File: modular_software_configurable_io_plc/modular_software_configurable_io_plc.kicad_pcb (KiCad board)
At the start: 4 copper layers, 105 x 107 mm, 38 parts, among them J1 FW-14-03-G-D-085-155, J10 CLP-108-02-G-D-BE, J11 CLP-102-02-G-D-BE, J12 CLP-102-02-G-D-BE, J13 CLP-102-02-G-D-BE, J14 CLP-108-02-G-D-BE, J15 FW-14-03-G-D-085-155, J16 FW-02-03-G-D-085-155, J17 FW-02-03-G-D-085-155, J18 FW-02-03-G-D-085-155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

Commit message: Backup
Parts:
- removed J23: TBP02R2-381, connector_footprints:TBP02R2-381-08BE
- moved J1 12.8 mm to (156.2, 103.3)
- moved J2 12.8 mm to (134.6, 106.4)
- moved J24 12.8 mm to (177.8, 122.3)
- moved J26 12.8 mm to (171.4, 107.7)
- moved J27 12.8 mm to (141.0, 107.7)
- moved J29 12.8 mm to (134.6, 122.3)
- moved J3 12.8 mm to (177.8, 106.4)
- moved J4 12.8 mm to (134.6, 115.3)
- moved J5 12.8 mm to (177.8, 115.3)
- moved J6 12.8 mm to (134.6, 129.3)
- moved J7 12.8 mm to (177.8, 129.3)
- moved J8 12.8 mm to (156.2, 139.4)
- moved J25 12.8 mm to (171.4, 131.8)
- moved J28 12.8 mm to (141.0, 131.8)
- moved MOD1 12.8 mm to (156.2, 117.9)
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
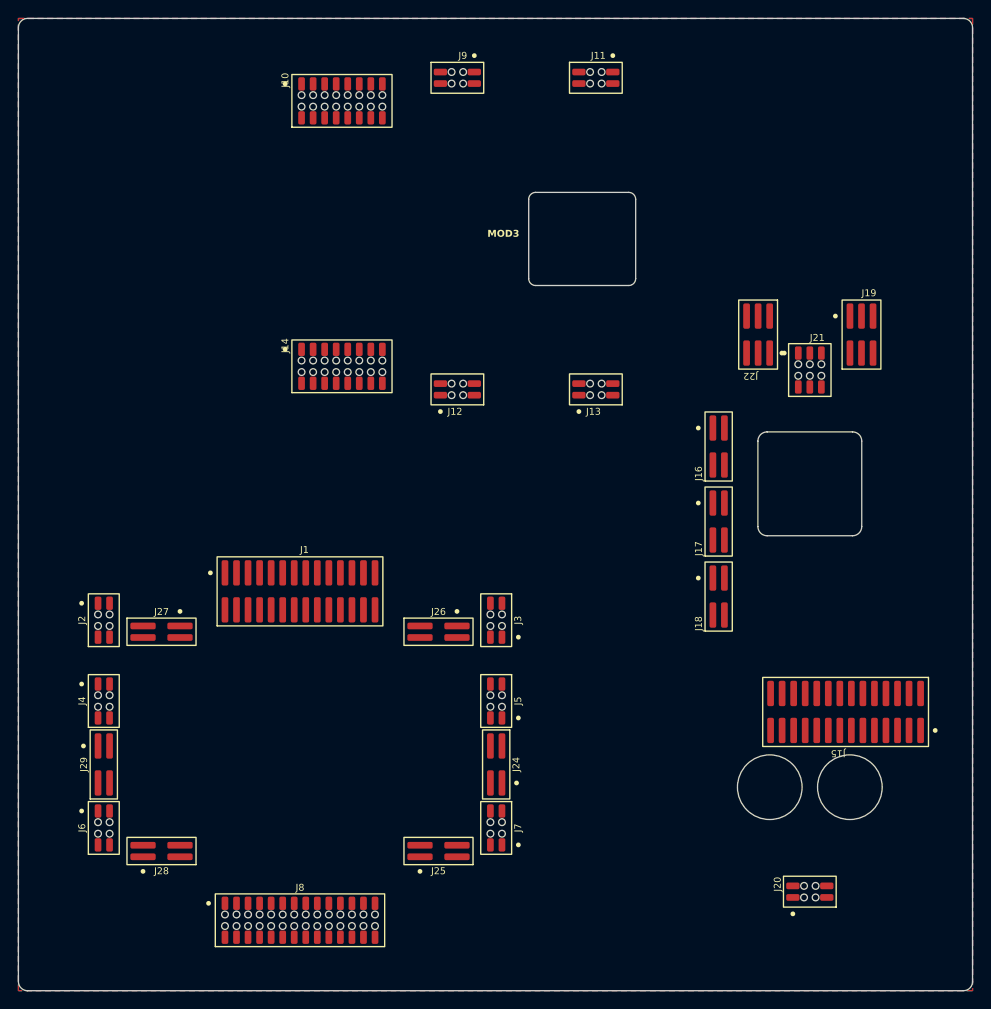
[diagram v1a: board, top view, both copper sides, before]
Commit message: Update KiCAD Symbol Generator submodule and add new mechanical component symbols
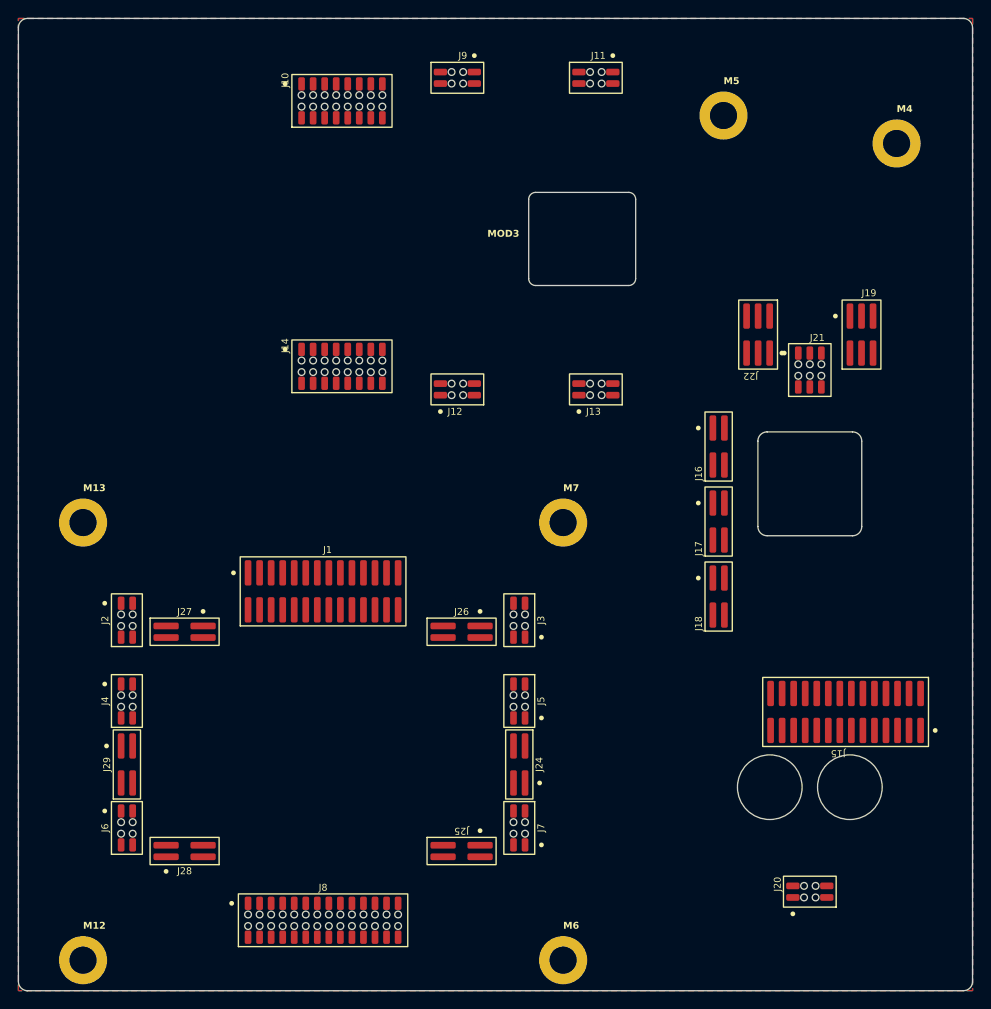
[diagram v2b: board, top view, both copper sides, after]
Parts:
- added M12: ~, mechanical_parts:9774020243R, F.Cu at (132.3, 143.8)
- added M13: ~, mechanical_parts:9774020243R, F.Cu at (132.3, 95.7)
- added M4: ~, mechanical_parts:9774020243R, F.Cu at (221.9, 54.0)
- added M5: ~, mechanical_parts:9774020243R, F.Cu at (202.8, 50.9)
- added M6: ~, mechanical_parts:9774020243R, F.Cu at (185.2, 143.8)
- added M7: ~, mechanical_parts:9774020243R, F.Cu at (185.2, 95.7)
- moved J25 2.54 mm to (174.0, 131.8), turned to -90 degrees
- moved J26 2.54 mm to (174.0, 107.7)
- moved J1 2.54 mm to (158.8, 103.3)
- moved J2 2.54 mm to (137.2, 106.4)
- moved J24 2.54 mm to (180.3, 122.3)
- moved J27 2.54 mm to (143.5, 107.7)
- moved J28 2.54 mm to (143.5, 131.8)
- moved J29 2.54 mm to (137.2, 122.3)
- moved J3 2.54 mm to (180.3, 106.4)
- moved J4 2.54 mm to (137.2, 115.3)
- moved J5 2.54 mm to (180.3, 115.3)
- moved J6 2.54 mm to (137.2, 129.3)
- moved J7 2.54 mm to (180.3, 129.3)
- moved J8 2.54 mm to (158.8, 139.4)
- moved MOD1 2.54 mm to (158.8, 117.9)
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
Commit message: Update modular software configurable IO PLC binary file
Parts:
- moved J1 1.80 mm to (157.5, 102.0)
- moved J6 1.80 mm to (135.9, 128.0)
- moved J7 1.80 mm to (179.1, 128.0)
- moved J8 1.80 mm to (157.5, 138.2)
- moved M12 1.80 mm to (131.1, 142.6)
- moved M6 1.80 mm to (183.9, 142.6)
- moved J2 1.80 mm to (135.9, 105.2)
- moved J24 1.80 mm to (179.1, 121.0)
- moved J26 1.80 mm to (172.7, 106.4)
- moved J29 1.80 mm to (135.9, 121.0)
- moved J3 1.80 mm to (179.1, 105.2)
- moved J4 1.80 mm to (135.9, 114.0)
- moved J5 1.80 mm to (179.1, 114.0)
- moved M13 1.80 mm to (131.1, 94.4)
- moved M7 1.80 mm to (183.9, 94.4)
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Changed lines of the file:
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@@
 	(footprint "connector_footprints:FW-02-03-G-D-085-155"
 		(layer "F.Cu")
-		(at 180.34 122.301 180)
+		(at 179.07 121.031 180)
 		(property "Reference" "J24"
 			(at -1.754 0 90)
@@
 	(footprint "mechanical_parts:9774020243R"
 		(layer "F.Cu")
-		(at 132.334 143.8402)
+		(at 131.064 142.5702)
 		(property "Reference" "M12"
 			(at 0 -3.81 0)
@@
 	(footprint "connector_footprints:FW-02-03-G-D-085-155"
 		(layer "F.Cu")
-		(at 143.51 107.696 -90)
+		(at 142.24 106.426 -90)
 		(property "Reference" "J27"
 			(at -1.754 0 0)
@@
 	(footprint "mechanical_parts:9774020243R"
 		(layer "F.Cu")
-		(at 185.166 95.6818)
+		(at 183.896 94.4118)
 		(property "Reference" "M7"
 			(at 0 -3.81 0)
@@
 	(footprint "connector_footprints:CLP-102-02-G-D-BE"
 		(layer "F.Cu")
-		(at 137.16 129.286)
+		(at 135.89 128.016)
 		(property "Reference" "J6"
 			(at -1.954 0 90)
@@
 	(footprint "modules_footprints:minimal_ad74413r"
 		(layer "F.Cu")
-		(at 158.75 117.856)
+		(at 157.48 116.586)
 		(property "Reference" "MOD1"
 			(at 0 -0.5 0)
@@
 	(footprint "connector_footprints:FW-14-03-G-D-085-155"
 		(layer "F.Cu")
-		(at 158.75 103.251)
+		(at 157.48 101.981)
 		(property "Reference" "J1"
 			(at 0 -4.572 0)
@@
 	(footprint "connector_footprints:CLP-102-02-G-D-BE"
 		(layer "F.Cu")
-		(at 180.34 115.316 180)
+		(at 179.07 114.046 180)
 		(property "Reference" "J5"
 			(at -1.954 0 90)
@@
 	(footprint "connector_footprints:FW-02-03-G-D-085-155"
 		(layer "F.Cu")
-		(at 143.51 131.826 90)
+		(at 142.24 130.556 90)
 		(property "Reference" "J28"
 			(at -1.754 0 0)
@@
 	(footprint "modules_footprints:minimal_max14906"
 		(layer "F.Cu")
-		(at 158.75 119.761)
+		(at 157.48 118.491)
 		(property "Reference" "MOD2"
 			(at 0 -0.5 0)
@@
 	(footprint "mechanical_parts:9774020243R"
 		(layer "F.Cu")
-		(at 132.334 95.681799)
+		(at 131.064 94.411799)
 		(property "Reference" "M13"
 			(at 0 -3.81 0)
@@
 	(footprint "connector_footprints:CLP-102-02-G-D-BE"
 		(layer "F.Cu")
-		(at 180.34 106.426 180)
+		(at 179.07 105.156 180)
 		(property "Reference" "J3"
 			(at -1.954 0 90)
@@
 	(footprint "connector_footprints:FW-02-03-G-D-085-155"
 		(layer "F.Cu")
-		(at 137.16 122.301)
+		(at 135.89 121.031)
 		(property "Reference" "J29"
 			(at -1.754 0 90)
@@
 	(footprint "connector_footprints:CLP-114-02-G-D-BE"
 		(layer "F.Cu")
-		(at 158.75 139.446)
+		(at 157.48 138.176)
 		(property "Reference" "J8"
 			(at 0 -3.154 0)
@@
 	(footprint "connector_footprints:CLP-102-02-G-D-BE"
 		(layer "F.Cu")
-		(at 180.34 129.286 180)
+		(at 179.07 128.016 180)
 		(property "Reference" "J7"
 			(at -1.954 0 90)
@@
 	(footprint "connector_footprints:FW-02-03-G-D-085-155"
 		(layer "F.Cu")
-		(at 173.99 131.826 -90)
+		(at 172.72 130.556 -90)
 		(property "Reference" "J25"
 			(at -1.754 0 180)
@@
 	(footprint "mechanical_parts:9774020243R"
 		(layer "F.Cu")
-		(at 185.166 143.8402)
+		(at 183.896 142.5702)
 		(property "Reference" "M6"
 			(at 0 -3.81 0)
@@
 	(footprint "connector_footprints:CLP-102-02-G-D-BE"
 		(layer "F.Cu")
-		(at 137.16 106.426)
+		(at 135.89 105.156)
 		(property "Reference" "J2"
 			(at -1.954 0 90)
@@
 	(footprint "connector_footprints:FW-02-03-G-D-085-155"
 		(layer "F.Cu")
-		(at 173.99 107.696 -90)
+		(at 172.72 106.426 -90)
 		(property "Reference" "J26"
 			(at -1.754 0 0)
@@
 	(footprint "connector_footprints:CLP-102-02-G-D-BE"
 		(layer "F.Cu")
-		(at 137.16 115.316)
+		(at 135.89 114.046)
 		(property "Reference" "J4"
 			(at -1.954 0 90)

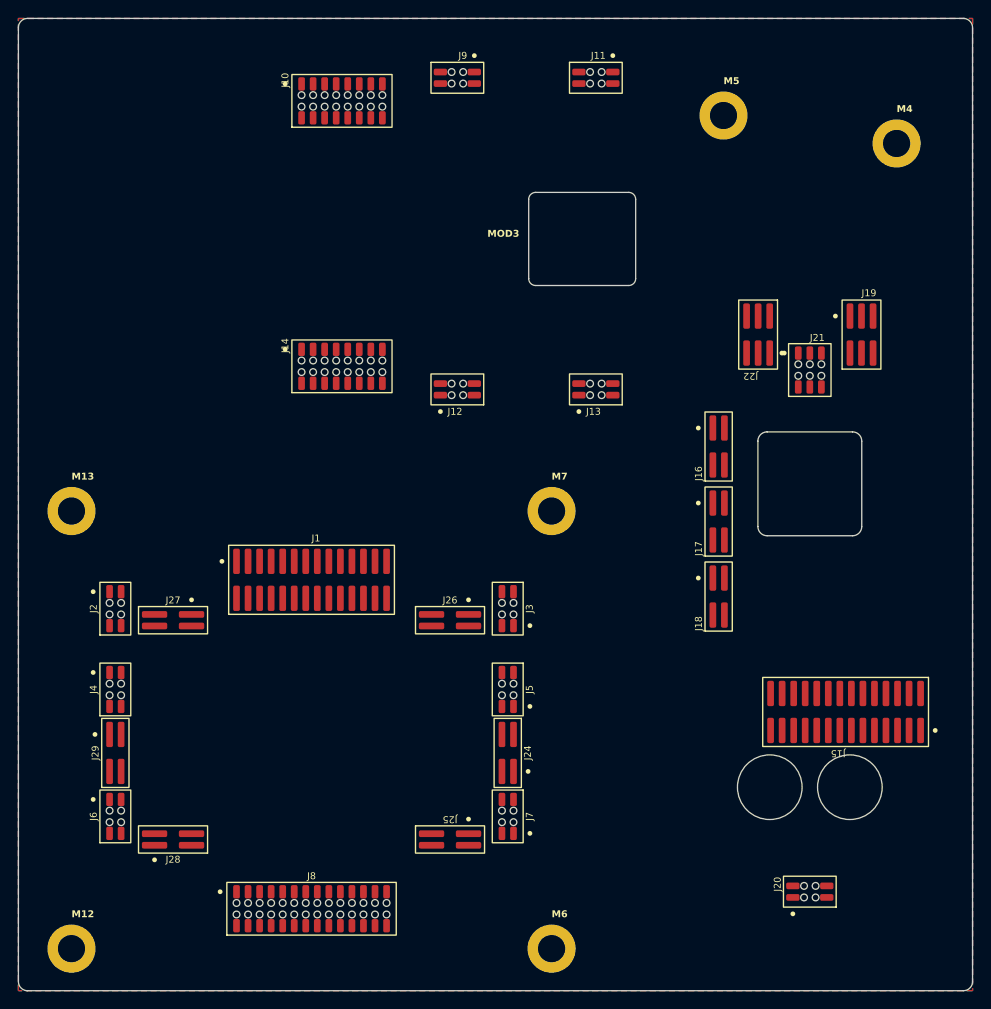
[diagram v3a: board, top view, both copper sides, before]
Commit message: Update KiCAD Symbol Generator submodule to latest commit
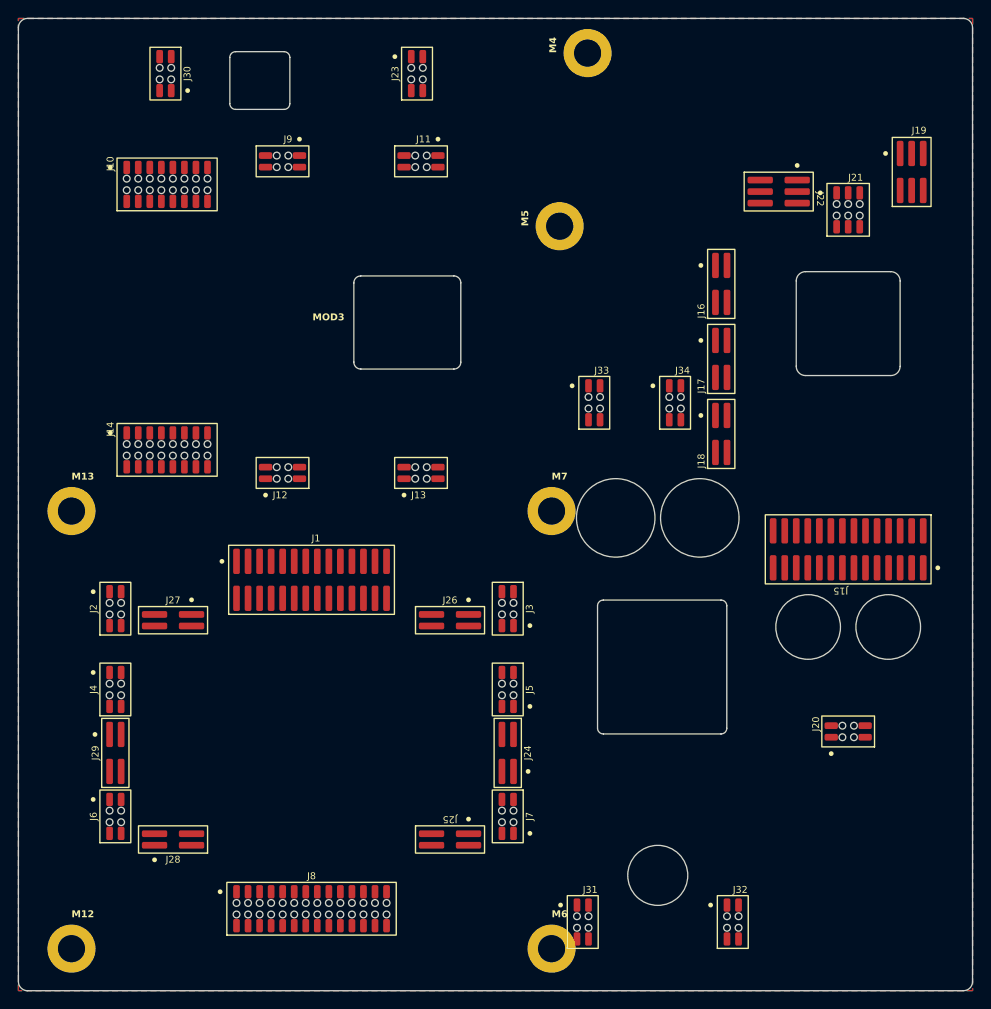
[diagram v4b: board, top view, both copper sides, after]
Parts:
- added J23: CLP-102-02-G-D-BE, connector_footprints:CLP-102-02-G-D-BE, F.Cu at (169.1, 46.3)
- added J30: CLP-102-02-G-D-BE, connector_footprints:CLP-102-02-G-D-BE, F.Cu at (141.4, 46.3)
- added J31: CLP-102-02-G-D-BE, connector_footprints:CLP-102-02-G-D-BE, F.Cu at (187.3, 139.6)
- added J32: CLP-102-02-G-D-BE, connector_footprints:CLP-102-02-G-D-BE, F.Cu at (203.8, 139.6)
- added J33: CLP-102-02-G-D-BE, connector_footprints:CLP-102-02-G-D-BE, F.Cu at (188.6, 82.5)
- added J34: CLP-102-02-G-D-BE, connector_footprints:CLP-102-02-G-D-BE, F.Cu at (197.5, 82.5)
- added MOD7: ~, modules_footprints:minimal_max17761, F.Cu at (155.2, 46.3)
- added MOD8: ~, modules_footprints:minimal_lt8304, F.Cu at (195.6, 112.2)
- moved M4 35.4 mm to (187.9, 44.0), turned to 90 degrees
- moved M5 21.8 mm to (184.8, 63.1), turned to 90 degrees
- moved J13 21.3 mm to (169.5, 90.2)
- moved J10 21.3 mm to (141.6, 58.5)
- moved J11 21.3 mm to (169.5, 55.9)
- moved J14 21.3 mm to (141.6, 87.7)
- moved MOD3 21.3 mm to (159.3, 73.1)
- moved J12 21.3 mm to (154.3, 90.2)
- moved J9 21.3 mm to (154.3, 55.9)
- moved MOD6 19.3 mm to (194.3, 53.5), turned to 0 degrees
- moved J19 18.7 mm to (223.5, 57.1)
- moved J21 18.1 mm to (216.5, 61.3)
- moved MOD5 18.1 mm to (216.5, 90.7)
- moved J20 18.1 mm to (216.5, 118.7)
- moved J16 17.9 mm to (202.6, 69.4)
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
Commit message: Backup
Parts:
- moved J30 40.1 mm to (135.4, 85.9), turned to -90 degrees
- moved J23 35.7 mm to (135.4, 58.2), turned to 90 degrees
- moved MOD7 32.5 mm to (135.4, 72.1), turned to -90 degrees
- moved J22 18.1 mm to (222.9, 47.8), turned to 90 degrees
- moved J10 14.9 mm to (155.5, 53.1)
- moved J14 14.9 mm to (155.5, 82.3)
- moved J12 14.9 mm to (168.2, 84.8)
- moved J9 14.9 mm to (168.2, 50.5)
- moved MOD6 12.7 mm to (207.0, 53.5)
- moved M5 11.5 mm to (196.2, 63.1)
- moved M4 11.5 mm to (199.3, 44.0)
- moved J11 10.4 mm to (178.4, 50.5)
- moved J13 10.4 mm to (178.4, 84.8)
- moved MOD3 10.4 mm to (168.2, 67.7)
- moved J27 1.27 mm to (141.2, 107.2)
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
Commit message: Update footprint library URIs to use KiCAD Symbols Generator
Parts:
- J19: value FW-02-03-G-D-085-155 -> FW-03-03-G-D-085-155
- J21: value CLP-102-02-G-D-BE -> CLP-103-02-G-D-BE

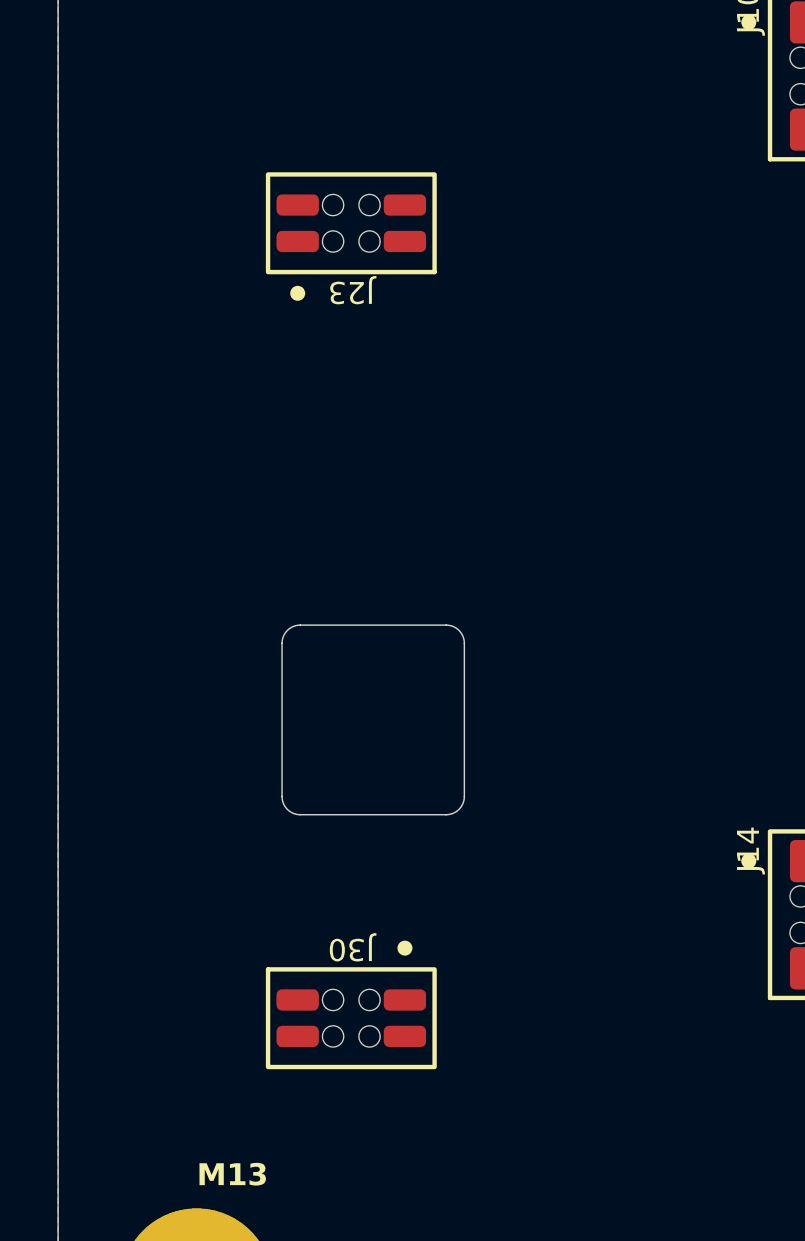
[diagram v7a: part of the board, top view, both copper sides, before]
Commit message: Update KiCAD Symbols Generator submodule reference
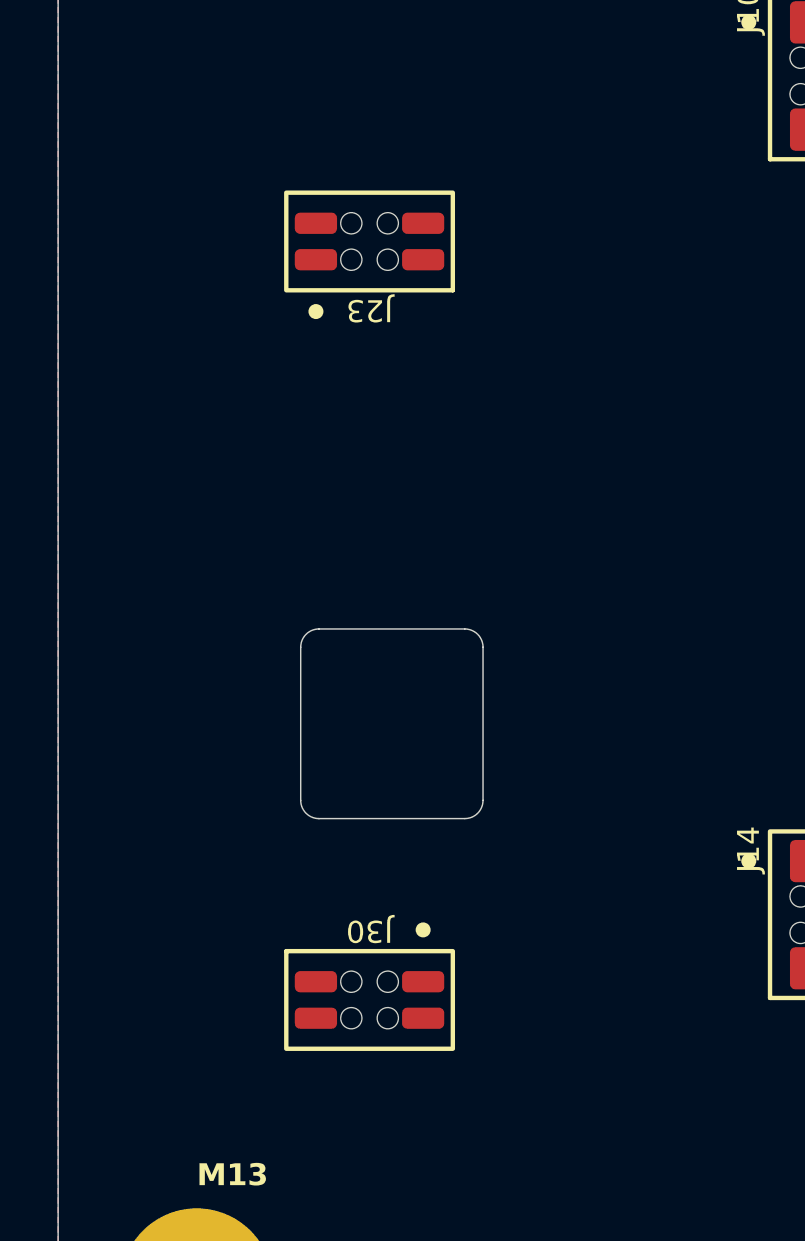
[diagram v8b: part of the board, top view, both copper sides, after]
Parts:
- moved J30 0.90 mm to (136.1, 85.3)
- moved J23 0.90 mm to (136.1, 58.9)
